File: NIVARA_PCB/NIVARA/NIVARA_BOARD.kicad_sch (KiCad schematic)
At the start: 0 parts

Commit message: kicad
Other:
- added sheet IN NPN (IN_NPN.kicad_sch)
- added sheet IN PNP (IN_PNP.kicad_sch)

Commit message: avance en diagramas
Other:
- added sheet fuente_alimentacion (fuente_alimentacion.kicad_sch)

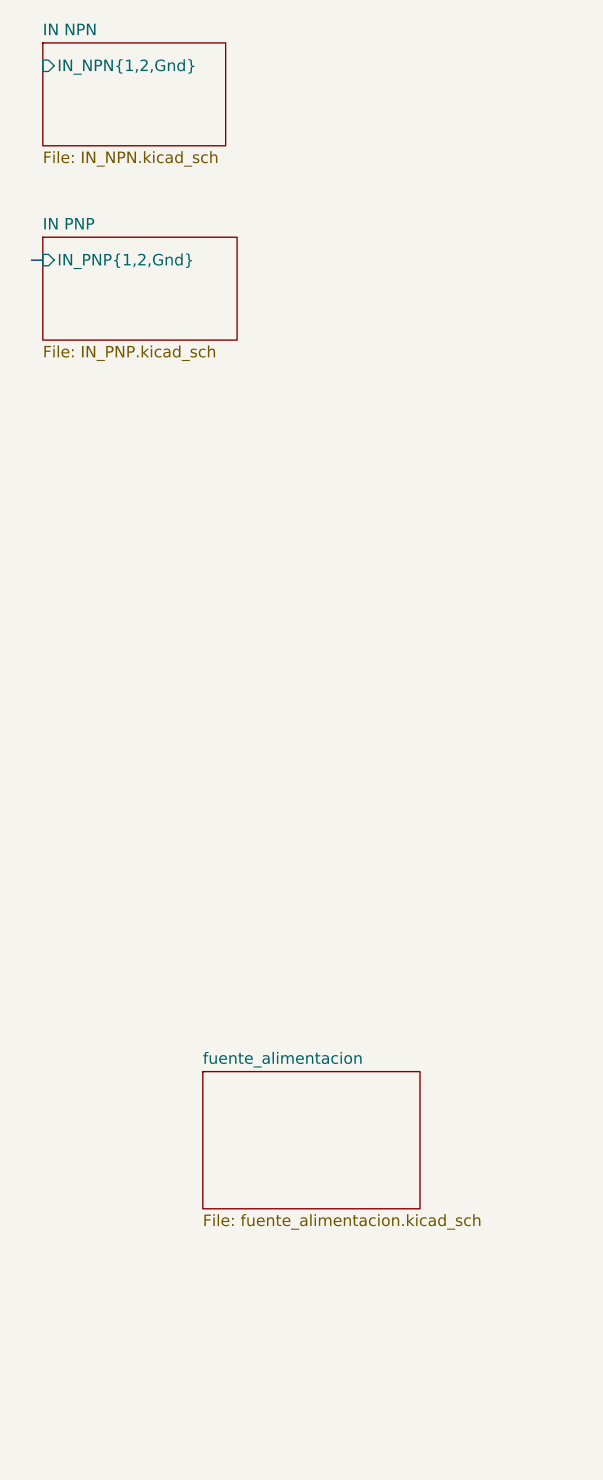
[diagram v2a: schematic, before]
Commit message: AVANCES
se realizaron avances con las entradas NPN, PNP. tambien se realizaron avances con las salidas de RELAYS
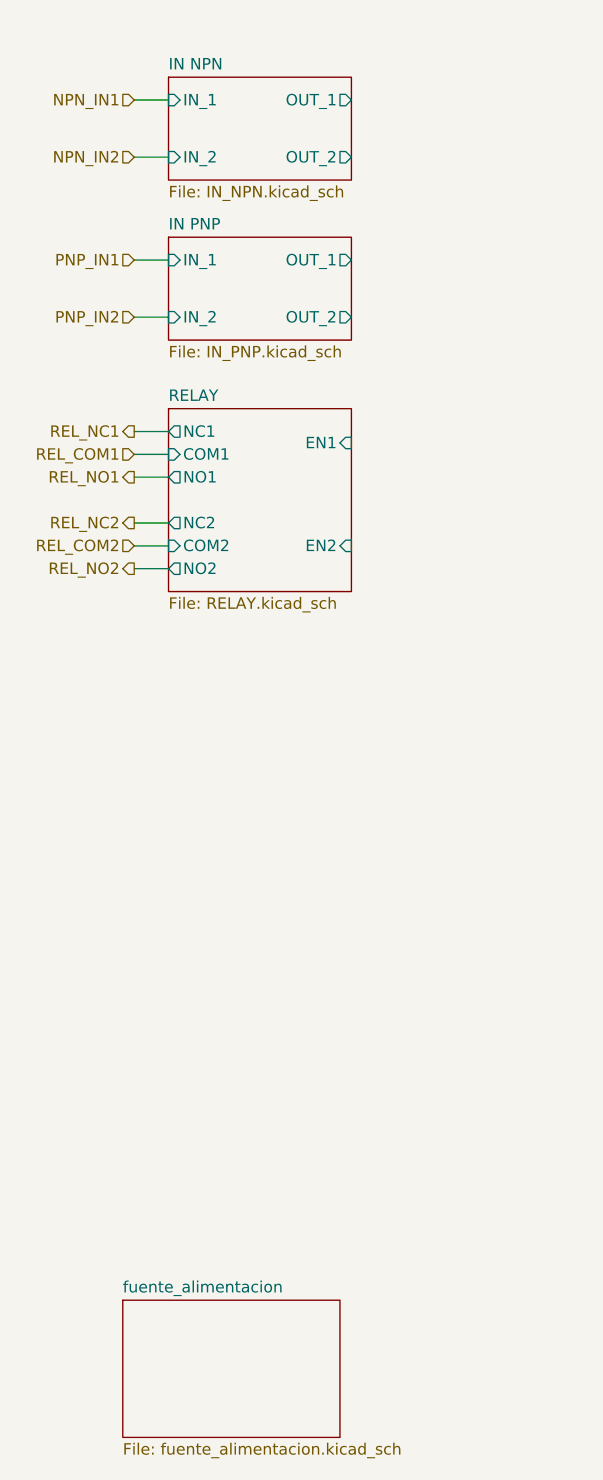
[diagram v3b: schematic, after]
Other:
- added sheet RELAY (RELAY.kicad_sch)
- sheet IN NPN ports: added IN_1, IN_2, OUT_1, OUT_2; removed IN_NPN{1,2,Gnd}
- sheet IN PNP ports: added IN_1, IN_2, OUT_1, OUT_2; removed IN_PNP{1,2,Gnd}

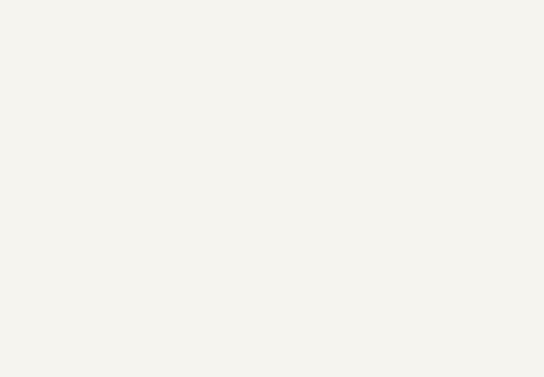
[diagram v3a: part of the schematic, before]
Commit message: RS_485 ADD MODULE
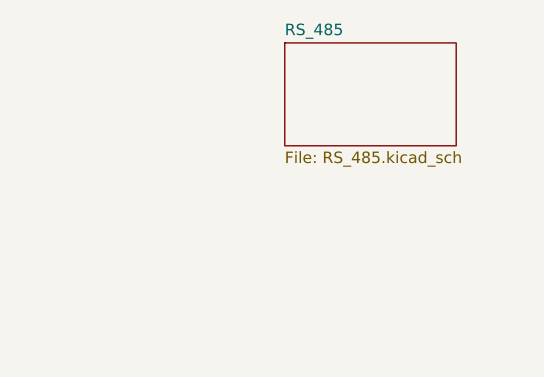
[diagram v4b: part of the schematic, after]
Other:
- added sheet RS_485 (RS_485.kicad_sch)
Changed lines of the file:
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@@
+	)
+	(sheet
+		(at 93.98 27.94)
+		(size 19.05 11.43)
+		(exclude_from_sim no)
+		(in_bom yes)
+		(on_board yes)
+		(dnp no)
+		(fields_autoplaced yes)
+		(stroke
+			(width 0.1524)
+			(type solid)
+		)
+		(fill
+			(color 0 0 0 0.0000)
+		)
+		(property "Sheetname" "RS_485"
+			(at 93.98 27.2284 0)
+			(effects
+				(font
+					(size 1.27 1.27)
+				)
+				(justify left bottom)
+			)
+		)
+		(property "Sheetfile" "RS_485.kicad_sch"
+			(at 93.98 39.9546 0)
+			(effects
+				(font
+					(size 1.27 1.27)
+				)
+				(justify left top)
+			)
+		)
+		(instances
+			(project "NIVARA"
+				(path "/6298d7d5-28da-40bf-9586-24a8e5c02b82/7ff0dada-fc46-483c-91ad-b264be8c64cf"
+					(page "7")
+				)
+			)
+		)
 	)
 	(sheet

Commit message: ACTUALIZACION
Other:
- sheet RS_485 ports: added A, B, RX, TX; removed none
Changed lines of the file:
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@@
+	(wire
+		(pts
+			(xy 146.05 33.02) (xy 147.32 33.02)
+		)
+		(stroke
+			(width 0)
+			(type default)
+		)
+	)
 	(wire
 		(pts
@@
 	(wire
 		(pts
+			(xy 146.05 36.83) (xy 147.32 36.83)
+		)
+		(stroke
+			(width 0)
+			(type default)
+		)
+	)
+	(wire
+		(pts
 			(xy 30.48 49.53) (xy 34.29 49.53)
 		)
@@
 			)
 			(justify right)
+		)
+	)
+	(hierarchical_label "RS_A"
+		(shape bidirectional)
+		(at 147.32 36.83 0)
+		(effects
+			(font
+				(size 1.27 1.27)
+			)
+			(justify left)
+		)
+	)
+	(hierarchical_label "RS_B"
+		(shape bidirectional)
+		(at 147.32 33.02 0)
+		(effects
+			(font
+				(size 1.27 1.27)
+			)
+			(justify left)
 		)
 	)
@@
 	)
 	(sheet
-		(at 29.21 165.1)
+		(at 29.21 167.64)
 		(size 24.13 15.24)
 		(exclude_from_sim no)
@@
 		)
 		(property "Sheetname" "fuente_alimentacion"
-			(at 29.21 164.3884 0)
+			(at 29.21 166.9284 0)
 			(effects
 				(font
@@
 		)
 		(property "Sheetfile" "fuente_alimentacion.kicad_sch"
-			(at 29.21 180.9246 0)
+			(at 29.21 183.4646 0)
 			(effects
 				(font
@@
 	)
 	(sheet
-		(at 93.98 27.94)
-		(size 19.05 11.43)
+		(at 125.73 29.21)
+		(size 20.32 11.43)
 		(exclude_from_sim no)
 		(in_bom yes)
@@
 		)
 		(property "Sheetname" "RS_485"
-			(at 93.98 27.2284 0)
+			(at 125.73 28.4984 0)
 			(effects
 				(font
@@
 		)
 		(property "Sheetfile" "RS_485.kicad_sch"
-			(at 93.98 39.9546 0)
+			(at 125.73 41.2246 0)
 			(effects
 				(font
@@
 			)
 		)
+		(pin "TX" bidirectional
+			(at 125.73 36.83 180)
+			(effects
+				(font
+					(size 1.27 1.27)
+				)
+				(justify left)
+			)
+		)
+		(pin "RX" bidirectional
+			(at 125.73 33.02 180)
+			(effects
+				(font
+					(size 1.27 1.27)
+				)
+				(justify left)
+			)
+		)
+		(pin "A" bidirectional
+			(at 146.05 36.83 0)
+			(effects
+				(font
+					(size 1.27 1.27)
+				)
+				(justify right)
+			)
+		)
+		(pin "B" bidirectional
+			(at 146.05 33.02 0)
+			(effects
+				(font
+					(size 1.27 1.27)
+				)
+				(justify right)
+			)
+		)

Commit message: ACTUALIZACION
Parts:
- added H1, H2: MountingHole_Pad, MountingHole:MountingHole_2.2mm_M2_Pad_Via, symbol Mechanical:MountingHole_Pad
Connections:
- new net GND: H1.1, H2.1
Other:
- added sheet IN D (IN_D.kicad_sch)
- added sheet OUT_NPN (OUT_NPN.kicad_sch)
- added sheet OUT_PNP (OUT_PNP.kicad_sch)

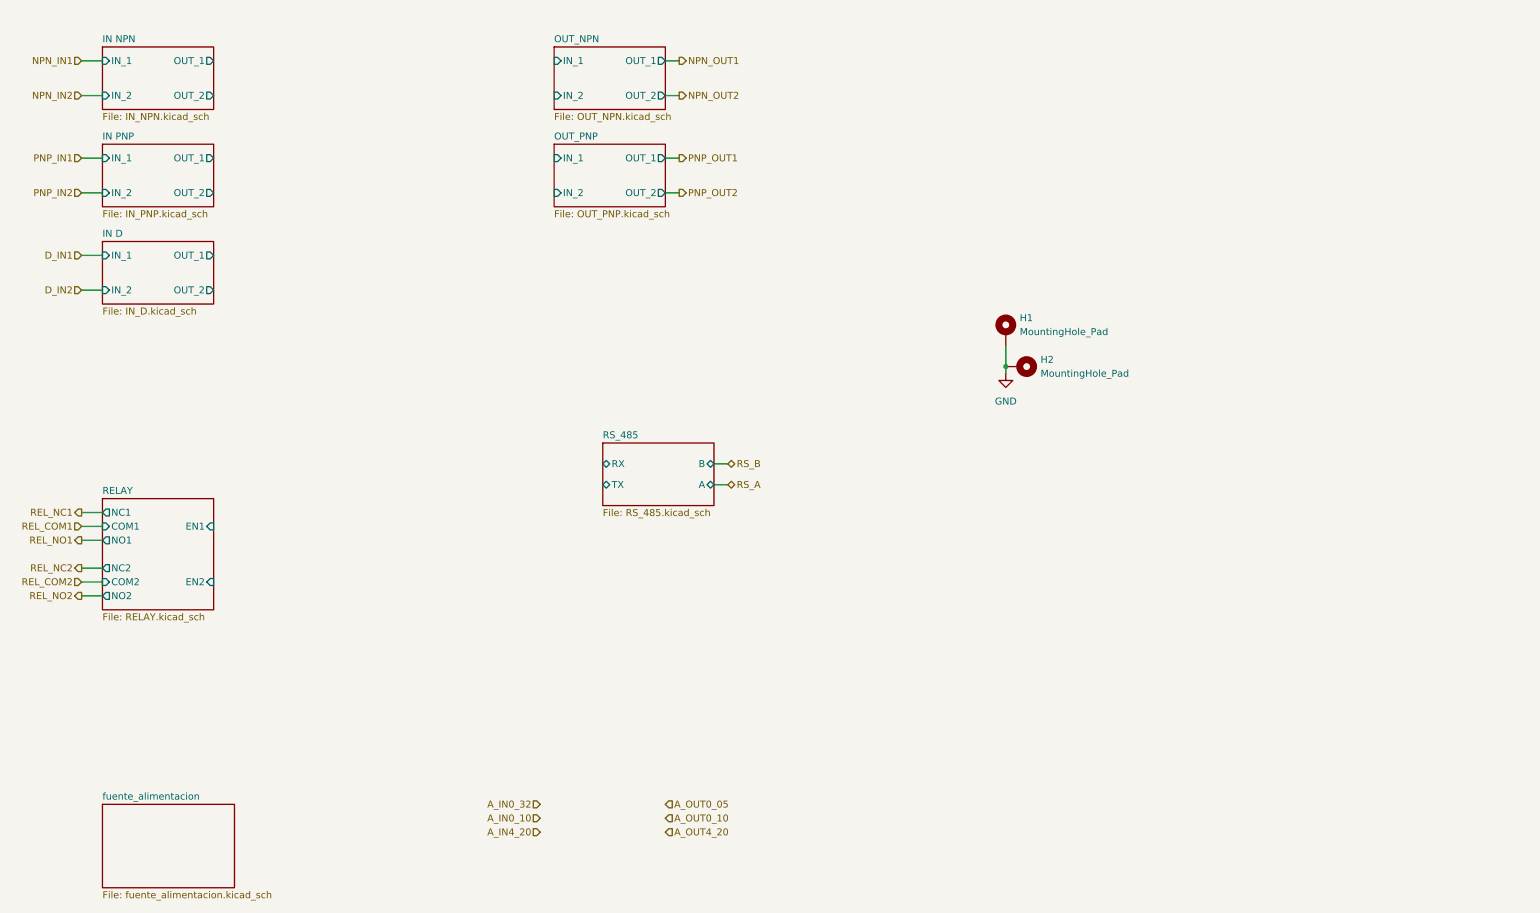
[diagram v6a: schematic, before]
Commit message: se agrego hirarchical de esp32 s3
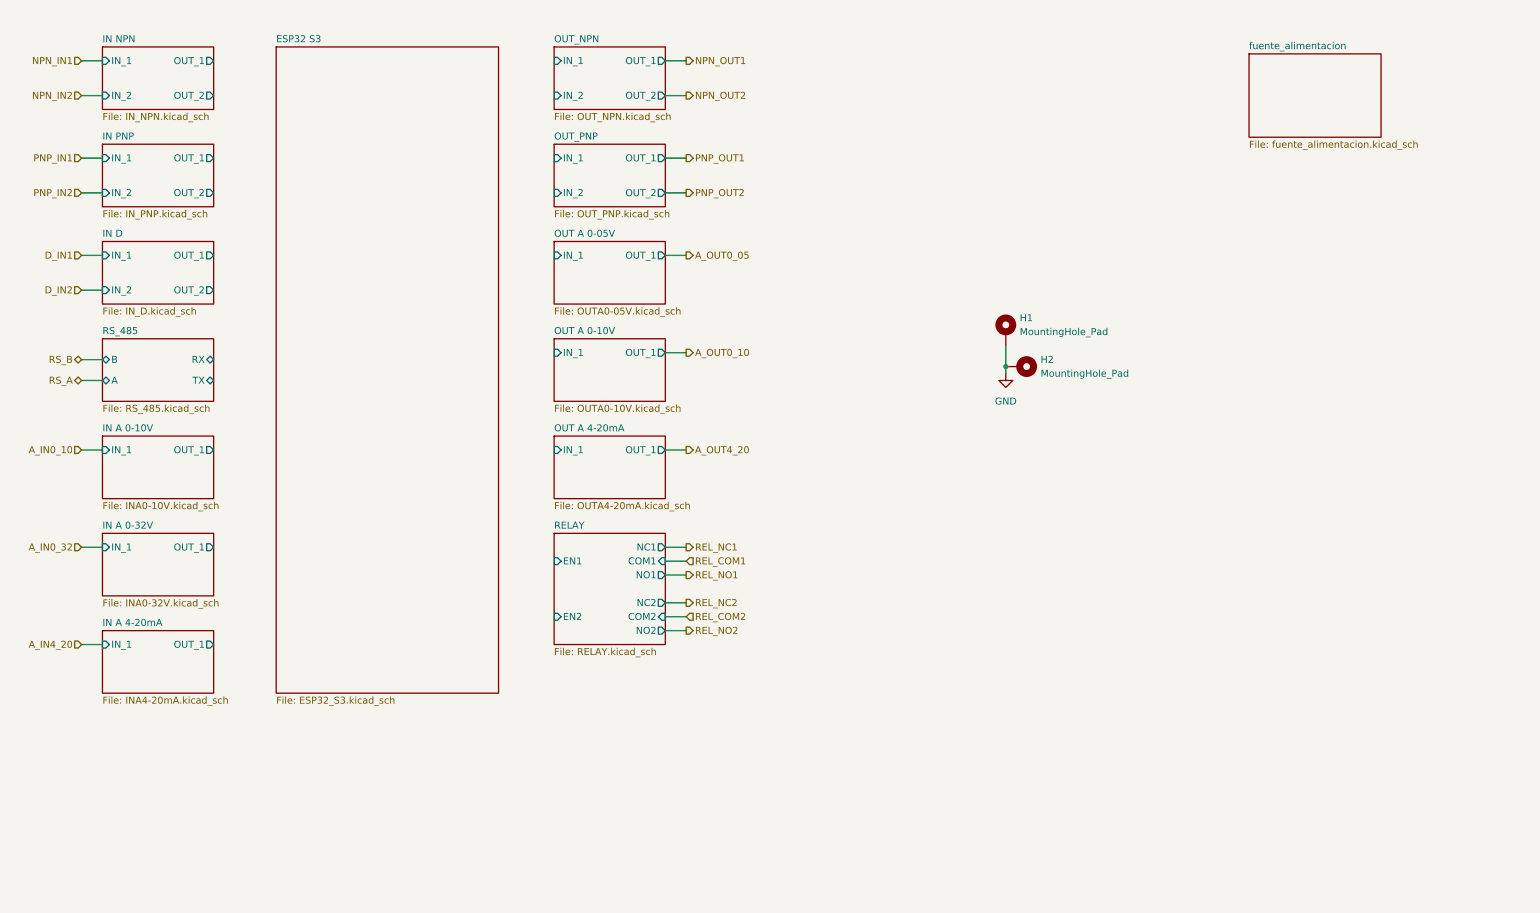
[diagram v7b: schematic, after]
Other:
- added sheet ESP32 S3 (ESP32_S3.kicad_sch)
- added sheet IN A 0-10V (INA0-10V.kicad_sch)
- added sheet IN A 0-32V (INA0-32V.kicad_sch)
- added sheet IN A 4-20mA (INA4-20mA.kicad_sch)
- added sheet OUT A 0-05V (OUTA0-05V.kicad_sch)
- added sheet OUT A 0-10V (OUTA0-10V.kicad_sch)
- added sheet OUT A 4-20mA (OUTA4-20mA.kicad_sch)

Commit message: avance
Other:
- sheet ESP32 S3 ports: added A_IN0_10, A_IN0_32, A_IN4_20, D_IN1, D_IN2, NPN_IN1, NPN_IN2, PNP_IN1, PNP_IN2, RX, TX; removed none
- moved on the sheet: H1, H2
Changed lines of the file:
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@@
 	(paper "A4")
 	(junction
-		(at 199.39 87.63)
+		(at 267.97 144.78)
 		(diameter 0)
 		(color 0 0 0 0)
@@
 	(wire
 		(pts
+			(xy 54.61 38.1) (xy 66.04 38.1)
+		)
+		(stroke
+			(width 0)
+			(type default)
+		)
+	)
+	(wire
+		(pts
+			(xy 54.61 67.31) (xy 66.04 67.31)
+		)
+		(stroke
+			(width 0)
+			(type default)
+		)
+	)
+	(wire
+		(pts
 			(xy 30.48 55.88) (xy 34.29 55.88)
 		)
@@
 	(wire
 		(pts
+			(xy 54.61 120.65) (xy 66.04 120.65)
+		)
+		(stroke
+			(width 0)
+			(type default)
+		)
+	)
+	(wire
+		(pts
+			(xy 54.61 73.66) (xy 66.04 73.66)
+		)
+		(stroke
+			(width 0)
+			(type default)
+		)
+	)
+	(wire
+		(pts
+			(xy 54.61 138.43) (xy 66.04 138.43)
+		)
+		(stroke
+			(width 0)
+			(type default)
+		)
+	)
+	(wire
+		(pts
 			(xy 140.97 125.73) (xy 137.16 125.73)
 		)
@@
 	(wire
 		(pts
+			(xy 54.61 86.36) (xy 66.04 86.36)
+		)
+		(stroke
+			(width 0)
+			(type default)
+		)
+	)
+	(wire
+		(pts
+			(xy 54.61 49.53) (xy 66.04 49.53)
+		)
+		(stroke
+			(width 0)
+			(type default)
+		)
+	)
+	(wire
+		(pts
 			(xy 30.48 138.43) (xy 34.29 138.43)
 		)
@@
 	(wire
 		(pts
-			(xy 199.39 87.63) (xy 199.39 88.9)
+			(xy 267.97 144.78) (xy 267.97 146.05)
 		)
 		(stroke
@@
 	(wire
 		(pts
+			(xy 54.61 31.75) (xy 66.04 31.75)
+		)
+		(stroke
+			(width 0)
+			(type default)
+		)
+	)
+	(wire
+		(pts
+			(xy 54.61 55.88) (xy 66.04 55.88)
+		)
+		(stroke
+			(width 0)
+			(type default)
+		)
+	)
+	(wire
+		(pts
 			(xy 30.48 38.1) (xy 34.29 38.1)
 		)
@@
 	(wire
 		(pts
+			(xy 54.61 102.87) (xy 66.04 102.87)
+		)
+		(stroke
+			(width 0)
+			(type default)
+		)
+	)
+	(wire
+		(pts
+			(xy 54.61 90.17) (xy 66.04 90.17)
+		)
+		(stroke
+			(width 0)
+			(type default)
+		)
+	)
+	(wire
+		(pts
 			(xy 34.29 90.17) (xy 30.48 90.17)
 		)
@@
 	(wire
 		(pts
-			(xy 199.39 83.82) (xy 199.39 87.63)
+			(xy 267.97 140.97) (xy 267.97 144.78)
 		)
 		(stroke
@@
 	(symbol
 		(lib_id "power:GND")
-		(at 199.39 88.9 0)
+		(at 267.97 146.05 0)
 		(unit 1)
 		(exclude_from_sim no)
@@
 		(fields_autoplaced yes)
 		(property "Reference" "#PWR08"
-			(at 199.39 95.25 0)
+			(at 267.97 152.4 0)
 			(effects
 				(font
@@
 		)
 		(property "Value" "GND"
-			(at 199.39 93.98 0)
+			(at 267.97 151.13 0)
 			(effects
 				(font
@@
 		)
 		(property "Footprint" ""
-			(at 199.39 88.9 0)
+			(at 267.97 146.05 0)
 			(effects
 				(font
@@
 		)
 		(property "Datasheet" ""
-			(at 199.39 88.9 0)
+			(at 267.97 146.05 0)
 			(effects
 				(font
@@
 		)
 		(property "Description" "Power symbol creates a global label with name \"GND\" , ground"
-			(at 199.39 88.9 0)
+			(at 267.97 146.05 0)
 			(effects
 				(font
@@
 	(symbol
 		(lib_id "Mechanical:MountingHole_Pad")
-		(at 201.93 87.63 270)
+		(at 270.51 144.78 270)
 		(unit 1)
 		(exclude_from_sim yes)
@@
 		(fields_autoplaced yes)
 		(property "Reference" "H2"
-			(at 205.74 86.3599 90)
+			(at 274.32 143.5099 90)
 			(effects
 				(font
@@
 		)
 		(property "Value" "MountingHole_Pad"
-			(at 205.74 88.8999 90)
+			(at 274.32 146.0499 90)
 			(effects
 				(font
@@
 		)
 		(property "Footprint" "MountingHole:MountingHole_2.2mm_M2_Pad_Via"
-			(at 201.93 87.63 0)
+			(at 270.51 144.78 0)
 			(effects
 				(font
@@
 		)
 		(property "Datasheet" "~"
-			(at 201.93 87.63 0)
+			(at 270.51 144.78 0)
 			(effects
 				(font
@@
 		)
 		(property "Description" "Mounting Hole with connection"
-			(at 201.93 87.63 0)
+			(at 270.51 144.78 0)
 			(effects
 				(font
@@
 	(symbol
 		(lib_id "Mechanical:MountingHole_Pad")
-		(at 199.39 81.28 0)
+		(at 267.97 138.43 0)
 		(unit 1)
 		(exclude_from_sim yes)
@@
 		(fields_autoplaced yes)
 		(property "Reference" "H1"
-			(at 201.93 78.7399 0)
+			(at 270.51 135.8899 0)
 			(effects
 				(font
@@
 		)
 		(property "Value" "MountingHole_Pad"
-			(at 201.93 81.2799 0)
+			(at 270.51 138.4299 0)
 			(effects
 				(font
@@
 		)
 		(property "Footprint" "MountingHole:MountingHole_2.2mm_M2_Pad_Via"
-			(at 199.39 81.28 0)
+			(at 267.97 138.43 0)
 			(effects
 				(font
@@
 		)
 		(property "Datasheet" "~"
-			(at 199.39 81.28 0)
+			(at 267.97 138.43 0)
 			(effects
 				(font
@@
 		)
 		(property "Description" "Mounting Hole with connection"
-			(at 199.39 81.28 0)
+			(at 267.97 138.43 0)
 			(effects
 				(font
@@
 			)
 		)
+		(pin "A_IN0_10" input
+			(at 66.04 102.87 180)
+			(effects
+				(font
+					(size 1.27 1.27)
+				)
+				(justify left)
+			)
+		)
+		(pin "D_IN2" input
+			(at 66.04 73.66 180)
+			(effects
+				(font
+					(size 1.27 1.27)
+				)
+				(justify left)
+			)
+		)
+		(pin "PNP_IN1" input
+			(at 66.04 49.53 180)
+			(effects
+				(font
+					(size 1.27 1.27)
+				)
+				(justify left)
+			)
+		)
+		(pin "D_IN1" input
+			(at 66.04 67.31 180)
+			(effects
+				(font
+					(size 1.27 1.27)
+				)
+				(justify left)
+			)
+		)
+		(pin "NPN_IN1" input
+			(at 66.04 31.75 180)
+			(effects
+				(font
+					(size 1.27 1.27)
+				)
+				(justify left)
+			)
+		)
+		(pin "NPN_IN2" input
+			(at 66.04 38.1 180)
+			(effects
+				(font
+					(size 1.27 1.27)
+				)
+				(justify left)
+			)
+		)
+		(pin "PNP_IN2" input
+			(at 66.04 55.88 180)
+			(effects
+				(font
+					(size 1.27 1.27)
+				)
+				(justify left)
+			)
+		)
+		(pin "A_IN4_20" input
+			(at 66.04 138.43 180)
+			(effects
+				(font
+					(size 1.27 1.27)
+				)
+				(justify left)
+			)
+		)
+		(pin "A_IN0_32" input
+			(at 66.04 120.65 180)
+			(effects
+				(font
+					(size 1.27 1.27)
+				)
+				(justify left)
+			)
+		)
+		(pin "TX" bidirectional
+			(at 66.04 90.17 180)
+			(effects
+				(font
+					(size 1.27 1.27)
+				)
+				(justify left)
+			)
+		)
+		(pin "RX" bidirectional
+			(at 66.04 86.36 180)
+			(effects
+				(font
+					(size 1.27 1.27)
+				)
+				(justify left)
+			)
+		)
